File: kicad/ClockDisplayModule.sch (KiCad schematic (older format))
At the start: 5 parts, among them IC101 ATMEGA8-P, P101 CONN_01X05, P102 CONN_02X03

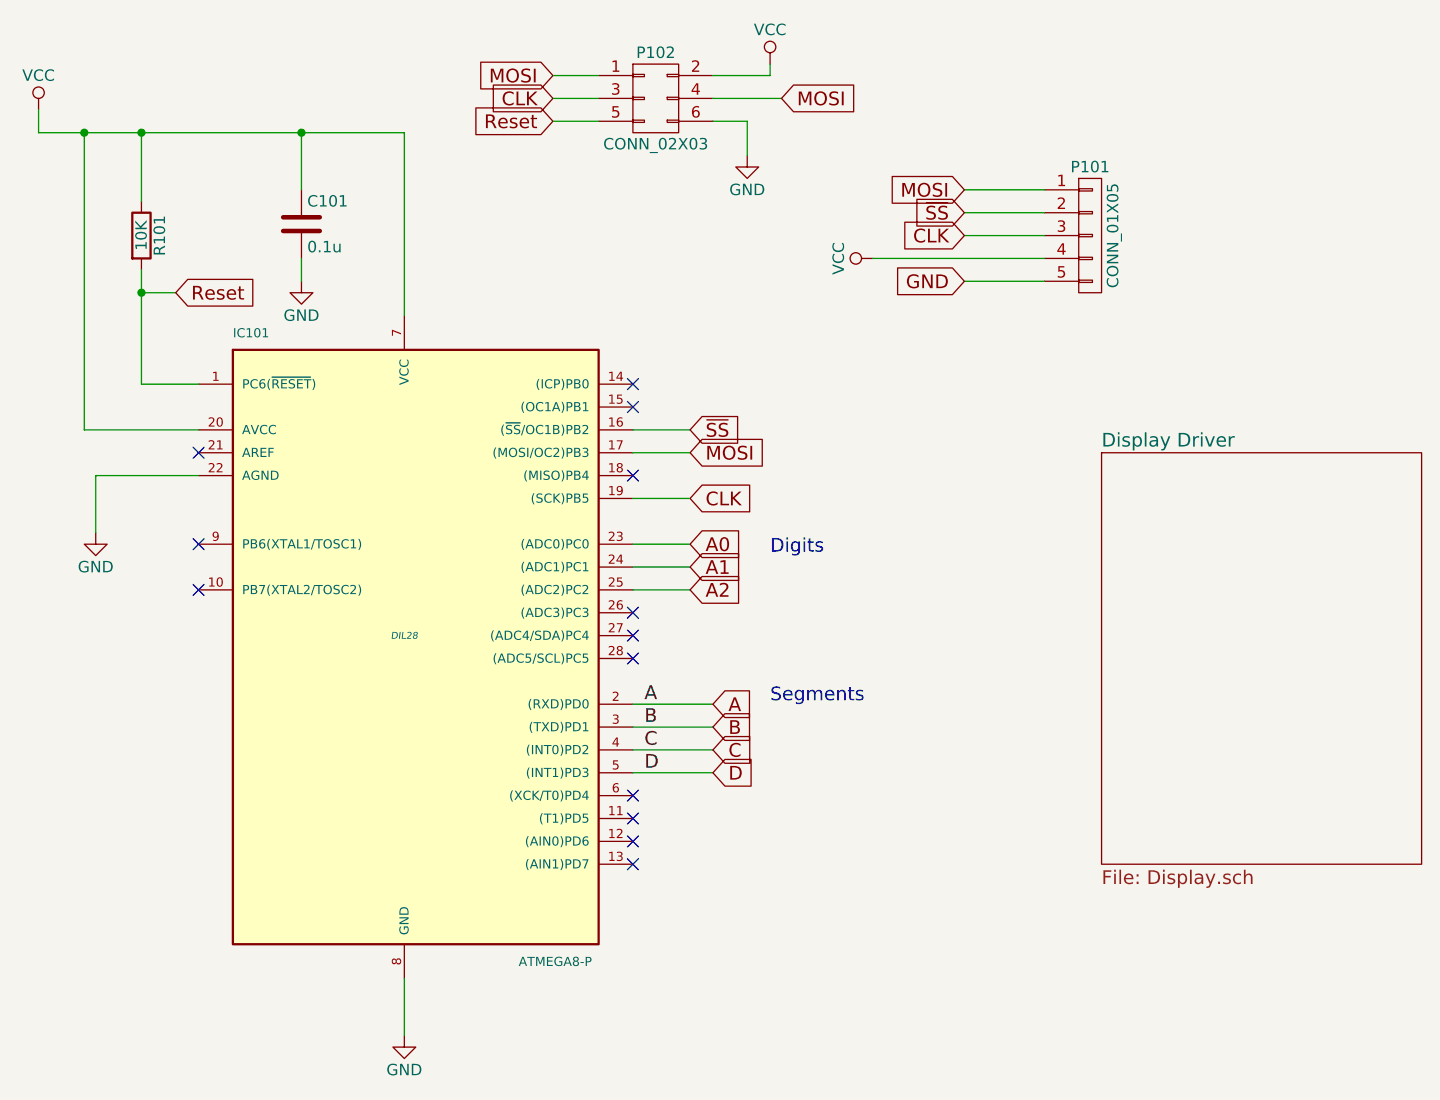
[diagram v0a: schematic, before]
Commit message: Started layout
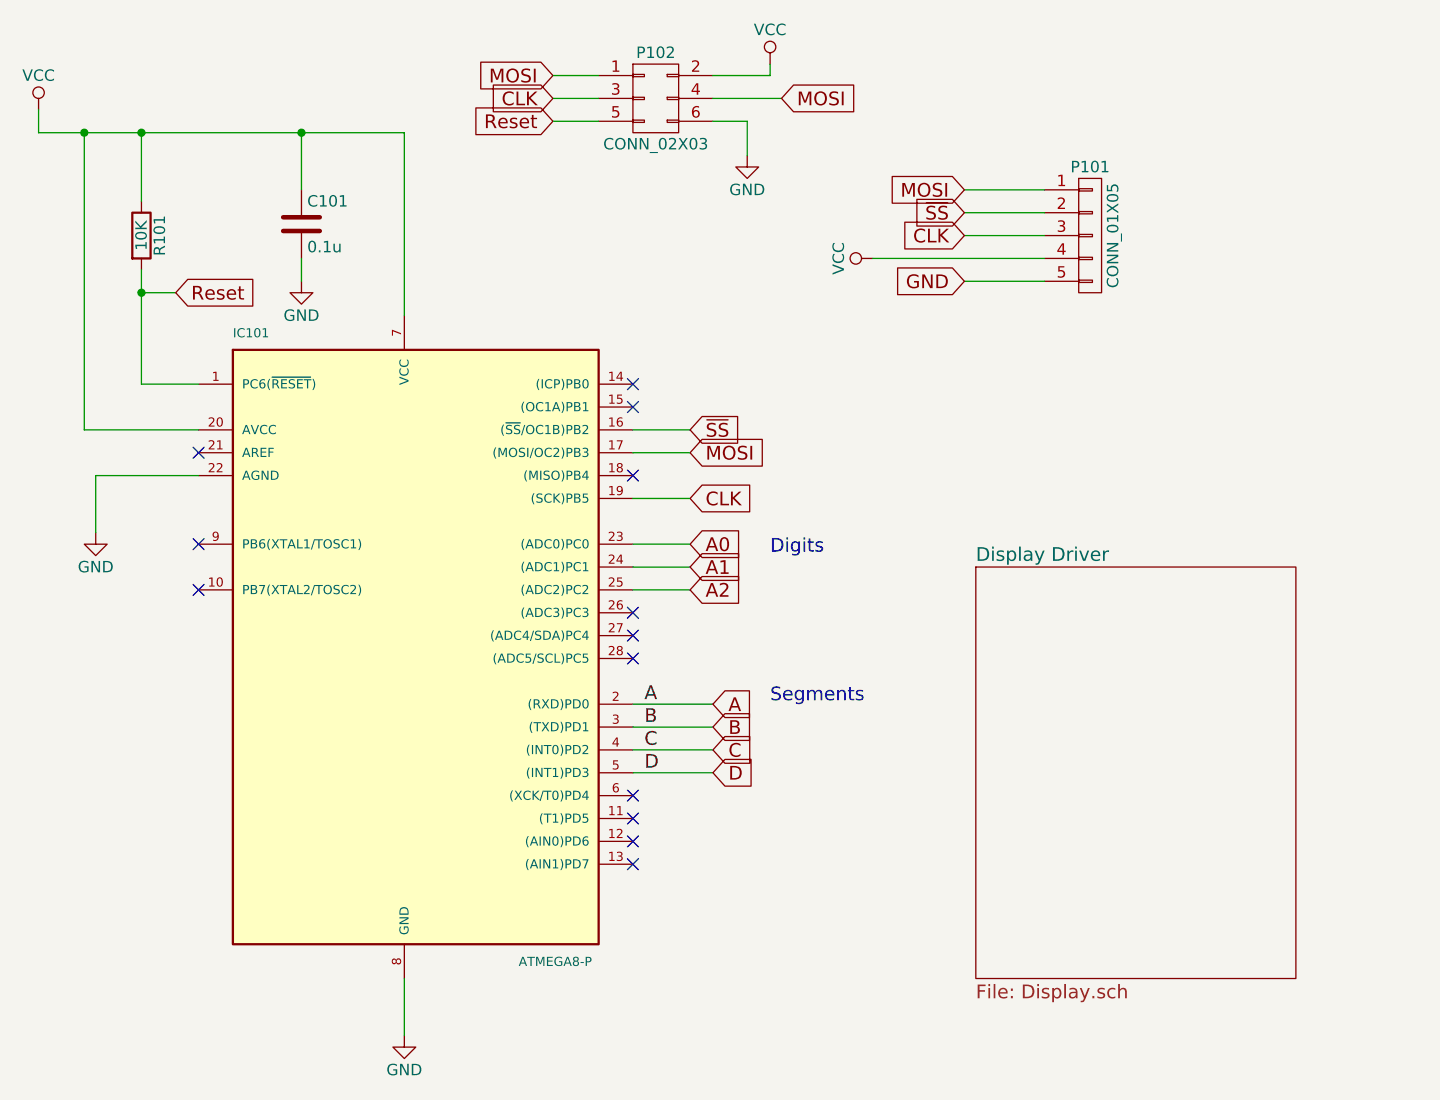
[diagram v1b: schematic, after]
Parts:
- IC101: footprint DIL28 -> Housings_QFP:TQFP-32_7x7mm_Pitch0.8mm
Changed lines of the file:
@@
 F 0 "IC101" H 3000 4700 40  0000 L BNN
 F 1 "ATMEGA8-P" H 4250 1950 40  0000 L BNN
-F 2 "DIL28" H 3750 3400 30  0000 C CIN
+F 2 "Housings_QFP:TQFP-32_7x7mm_Pitch0.8mm" H 3750 3400 30  0001 C CIN
 F 3 "" H 3750 3400 60  0000 C CNN
 F 4 "ATMEGA88PV-10AUR" H 3750 3400 60  0001 C CNN "MPN"
@@
 	4750 2500 5000 2500
 Wire Wire Line
-	2600 1800 2600 2300
+	2600 1800 2600 1900
+Wire Wire Line
+	2600 1900 2600 2300
 Wire Wire Line
 	2600 2300 2850 2300
 Wire Wire Line
-	2150 1200 3750 1200
+	2150 1200 2350 1200
+Wire Wire Line
+	2350 1200 2600 1200
+Wire Wire Line
+	2600 1200 3300 1200
+Wire Wire Line
+	3300 1200 3750 1200
 Wire Wire Line
 	3750 1200 3750 2000
@@
 A2
 $Sheet
-S 6800 2600 1400 1800
+S 6250 3100 1400 1800
 U 5587144A
 F0 "Display Driver" 60
